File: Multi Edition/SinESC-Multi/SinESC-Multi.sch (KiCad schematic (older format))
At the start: 84 parts, among them J1 Pad_3x2mm, J2 Pad_3x2mm, J3 Pad_3x2mm, J4 Pad_3x2mm, J5 Pad_3x2mm, J6 Pad_1.5mm_Square, Q1 BSC010N04LSI, Q2 BSC010N04LSI, Q3 BSC010N04LSI, Q4 BSC010N04LSI, Q5 BSC010N04LSI, Q6 BSC010N04LSI, U1 STM32F303CBT7, U2 MAX4239AUT, U3 MAX4239AUT, U4 TMC6100-LA, U5 MAX4239AUT, U6 TPS560430XDBVR, Y1 8MHz

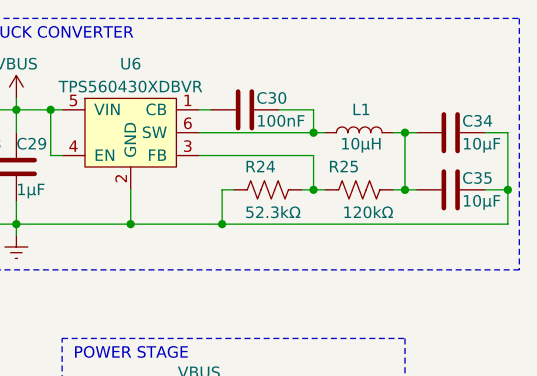
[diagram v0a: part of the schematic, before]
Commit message: Fix issue in the schematic in which the buck converter's 3.3V output is not connected to the rest of the 3.3V rail
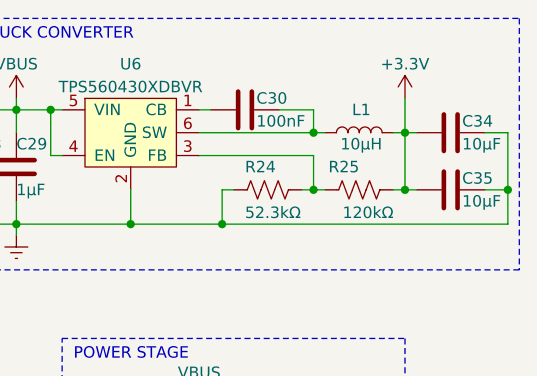
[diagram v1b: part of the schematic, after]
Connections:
- net +3V3: now also C34.2, C35.2, L1.2, R25.2
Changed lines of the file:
@@
 Sheet 1 1
 Title "SinESC Multi Edition"
-Date "2020-09-03"
-Rev "2.3B"
-Comp "Drawn by SAR_mango, © SinESC 2020"
-Comment1 "* All resistors are 1% 0201; current shunts are 1% 1206."
-Comment2 "* Capacitor voltage ratings & packages vary. See BOM."
-Comment3 "* Despite BOM consolidation, E192 values are required."
+Date "2020-12-28"
+Rev "2.3C"
+Comp "Drawn by Erk S., © 2020 SinESC"
+Comment1 "*All resistors are 1% 0201; current shunts are 1% 1206."
+Comment2 "*Capacitor voltage ratings & packages vary. See BOM."
+Comment3 "*Despite BOM consolidation, E192 values are required."
 Comment4 ""
 $EndDescr
@@
 EndData
 $EndBitmap
+$Comp
+L power:+3.3V #PWR?
+U 1 1 5FEB2144
+P 10050 850
+F 0 "#PWR?" H 10050 700 50  0001 C CNN
+F 1 "+3.3V" H 10050 1000 50  0000 C CNN
+F 2 "" H 10050 850 50  0001 C CNN
+F 3 "" H 10050 850 50  0001 C CNN
+	1    10050 850
+	1    0    0    -1
+$EndComp
+Wire Wire Line
+	10050 850  10050 1000
 $EndSCHEMATC

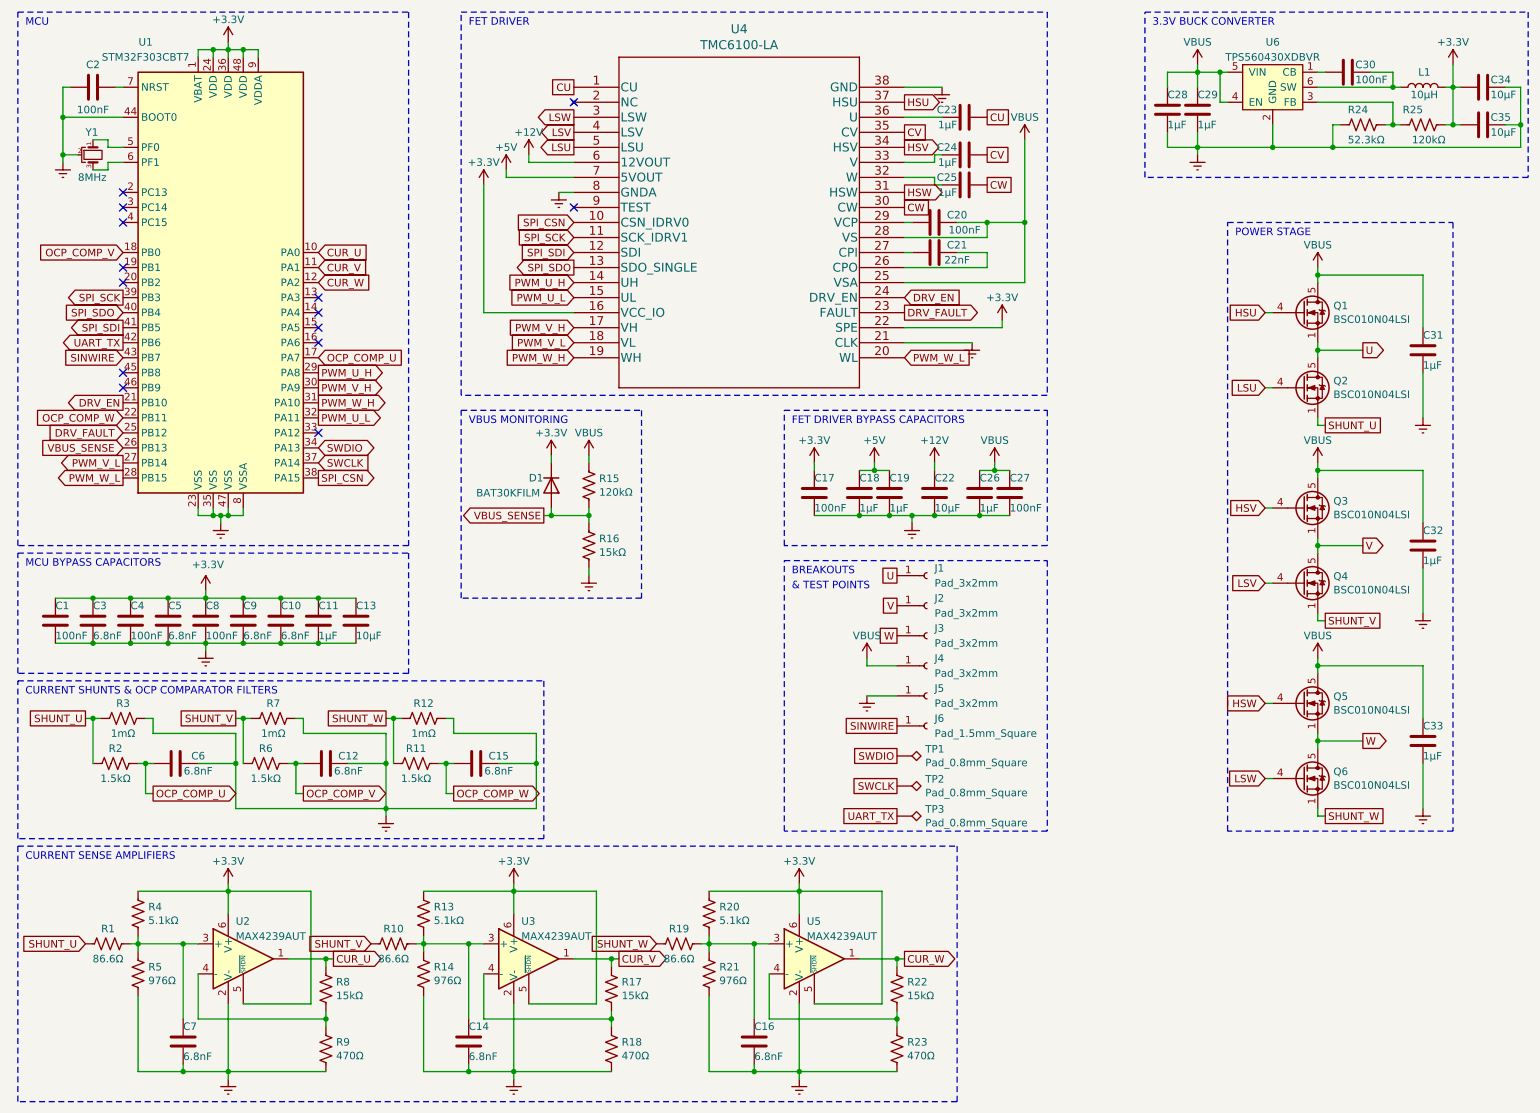
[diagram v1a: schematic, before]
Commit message: Fix another issue in which the bootstrap capacitors were not connected to the source pins of the high-side FETs
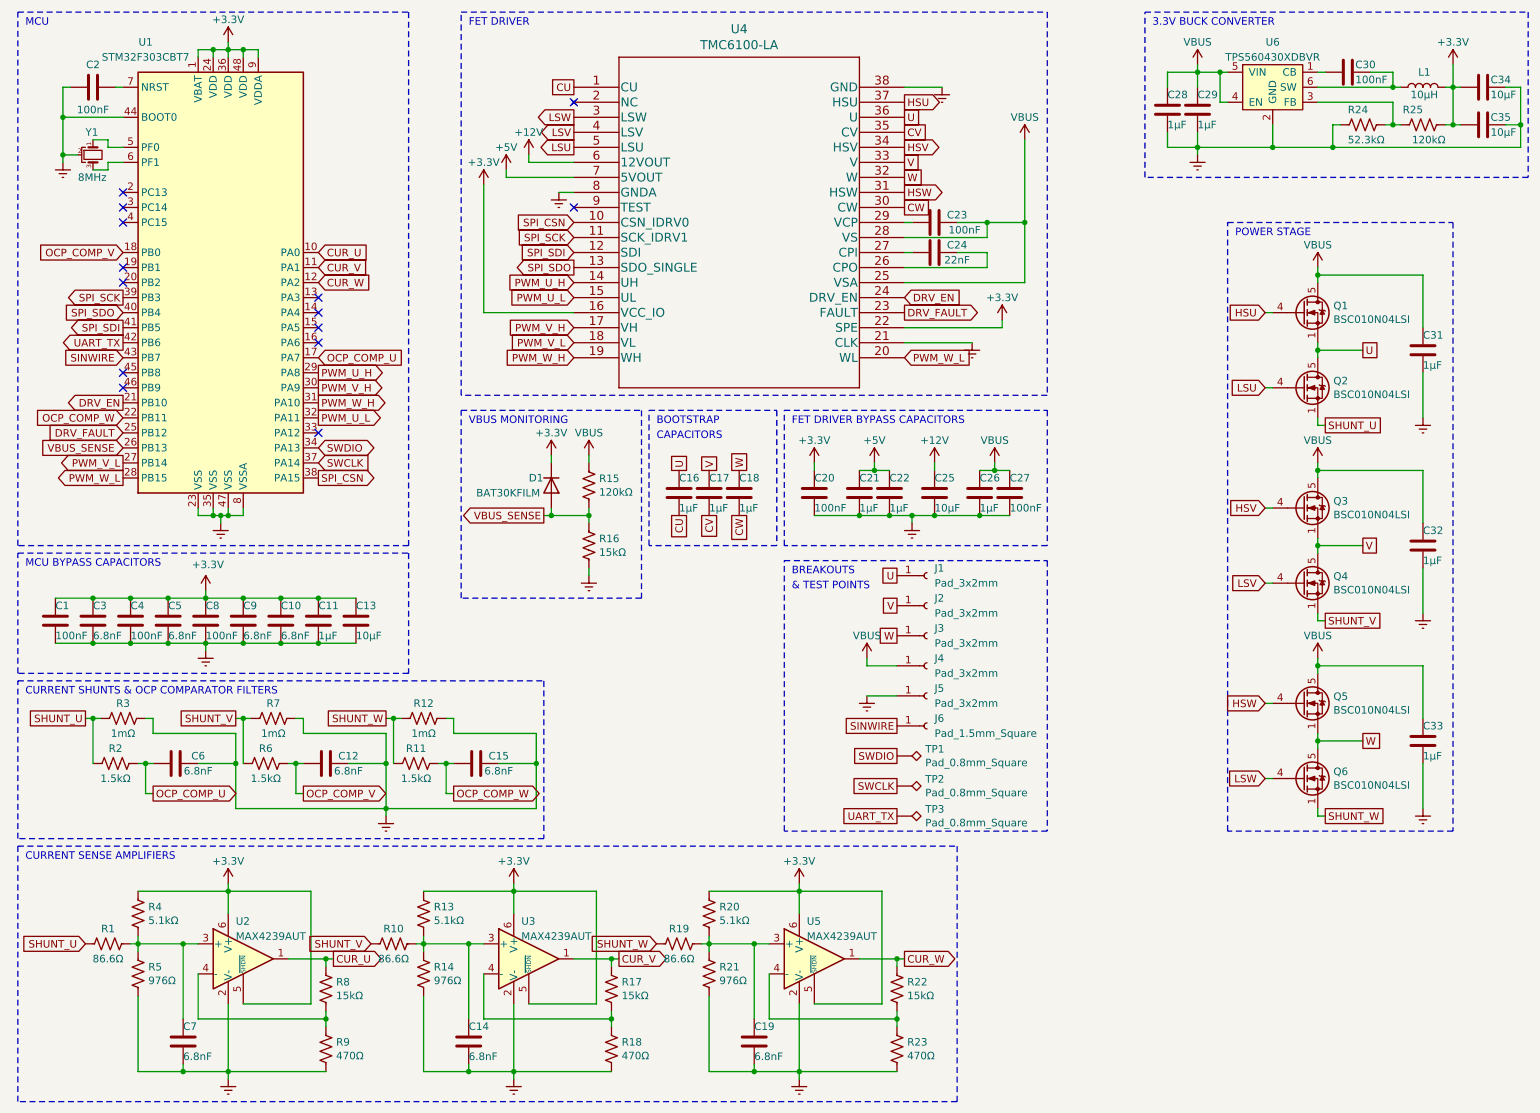
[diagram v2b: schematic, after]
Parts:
- U1: footprint Package_QFP:LQFP-48_7x7mm_P0.5mm -> LQFP-48_7x7mm_P0.5mm_narrow_pads:LQFP-48_7x7mm_P0.5mm_narrow_pads
- renumbered C23 to C16, C24 to C17, C25 to C18, C16 to C19, C17 to C20, C18 to C21, C19 to C22, C20 to C23, C21 to C24, C22 to C25
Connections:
- net U: now also C16.1, U4.36 (U)
- net V: now also C17.1, U4.33 (V)
- net W: now also C18.1, U4.32 (W)
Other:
- note added: "BOOTSTRAP"
- note added: "CAPACITORS"
- moved on the sheet: C16, C17, C18
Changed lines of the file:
@@
 Sheet 1 1
 Title "SinESC Multi Edition"
-Date "2020-12-28"
+Date "2020-12-30"
 Rev "2.3C"
 Comp "Drawn by Erk S., © 2020 SinESC"
@@
 $EndComp
 $Comp
-L Device:C C16
+L Device:C C19
 U 1 1 5F7BA4B1
 P 5400 7350
-F 0 "C16" H 5400 7450 50  0000 L CNN
+F 0 "C19" H 5400 7450 50  0000 L CNN
 F 1 "6.8nF" H 5400 7250 50  0000 L CNN
 F 2 "Capacitor_SMD:C_0201_0603Metric" H 5438 7200 50  0001 C CNN
@@
 $EndComp
 $Comp
-L Device:C C22
+L Device:C C25
 U 1 1 5F4CAC58
 P 6600 3700
-F 0 "C22" H 6600 3800 50  0000 L CNN
+F 0 "C25" H 6600 3800 50  0000 L CNN
 F 1 "10µF" H 6600 3600 50  0000 L CNN
 F 2 "Capacitor_SMD:C_0603_1608Metric" H 6638 3550 50  0001 C CNN
@@
 $EndComp
 $Comp
-L Device:C C19
+L Device:C C22
 U 1 1 5F4CAA4D
 P 6300 3700
-F 0 "C19" H 6300 3800 50  0000 L CNN
+F 0 "C22" H 6300 3800 50  0000 L CNN
 F 1 "1µF" H 6300 3600 50  0000 L CNN
 F 2 "Capacitor_SMD:C_0402_1005Metric" H 6338 3550 50  0001 C CNN
@@
 $EndComp
 $Comp
-L Device:C C18
+L Device:C C21
 U 1 1 5F4CA4EA
 P 6100 3700
-F 0 "C18" H 6100 3800 50  0000 L CNN
+F 0 "C21" H 6100 3800 50  0000 L CNN
 F 1 "1µF" H 6100 3600 50  0000 L CNN
 F 2 "Capacitor_SMD:C_0402_1005Metric" H 6138 3550 50  0001 C CNN
@@
 $EndComp
 $Comp
-L Device:C C17
+L Device:C C20
 U 1 1 5F4C9EF6
 P 5800 3700
-F 0 "C17" H 5800 3800 50  0000 L CNN
+F 0 "C20" H 5800 3800 50  0000 L CNN
 F 1 "100nF" H 5800 3600 50  0000 L CNN
 F 2 "Capacitor_SMD:C_0201_0603Metric" H 5838 3550 50  0001 C CNN
@@
 	6450 2100 6400 2100
 $Comp
-L Device:C C21
+L Device:C C24
 U 1 1 5F488471
 P 6600 2100
-F 0 "C21" V 6550 2250 50  0000 C CNN
+F 0 "C24" V 6550 2250 50  0000 C CNN
 F 1 "22nF" V 6650 2250 50  0000 C CNN
 F 2 "Capacitor_SMD:C_0603_1608Metric" H 6638 1950 50  0001 C CNN
@@
 	6450 1900 6400 1900
 $Comp
-L Device:C C20
+L Device:C C23
 U 1 1 5F47F307
 P 6600 1900
-F 0 "C20" V 6550 2050 50  0000 C CNN
+F 0 "C23" V 6550 2050 50  0000 C CNN
 F 1 "100nF" V 6650 2100 50  0000 C CNN
 F 2 "Capacitor_SMD:C_0201_0603Metric" H 6638 1750 50  0001 C CNN
@@
 Text GLabel 4200 1900 0    50   Input ~ 0
 SPI_CSN
-Wire Wire Line
-	6650 1650 6600 1650
-Wire Wire Line
-	6650 1450 6600 1450
-Wire Wire Line
-	6650 1200 6400 1200
 NoConn ~ 4200 1100
 $Comp
@@
 Text GLabel 4200 1200 0    50   Output ~ 0
 LSW
-Wire Wire Line
-	6600 1600 6400 1600
-Wire Wire Line
-	6600 1650 6600 1600
-Wire Wire Line
-	6600 1500 6600 1450
-Wire Wire Line
-	6400 1500 6600 1500
 Text GLabel 6400 1100 2    50   Output ~ 0
 HSU
@@
 HSV
 $Comp
-L Device:C C24
+L Device:C C17
 U 1 1 5F40C21D
-P 6800 1450
-F 0 "C24" V 6850 1500 50  0000 L CNN
-F 1 "1µF" V 6750 1500 50  0000 L CNN
-F 2 "Capacitor_SMD:C_0402_1005Metric" H 6838 1300 50  0001 C CNN
-F 3 "" H 6800 1450 50  0001 C CNN
-F 4 "50V" H 6800 1450 50  0001 C CNN "Voltage Rating"
-F 5 "UMK105CBJ105MV-F" H 6800 1450 50  0001 C CNN "Manufacturer Part #"
-	1    6800 1450
-	0    -1   -1   0
+P 5100 3700
+F 0 "C17" H 5100 3800 50  0000 L CNN
+F 1 "1µF" H 5100 3600 50  0000 L CNN
+F 2 "Capacitor_SMD:C_0402_1005Metric" H 5138 3550 50  0001 C CNN
+F 3 "" H 5100 3700 50  0001 C CNN
+F 4 "50V" H 5100 3700 50  0001 C CNN "Voltage Rating"
+F 5 "UMK105CBJ105MV-F" H 5100 3700 50  0001 C CNN "Manufacturer Part #"
+	1    5100 3700
+	1    0    0    -1
 $EndComp
-Text GLabel 6950 1450 2    50   UnSpc ~ 0
+Text GLabel 5100 3850 3    50   UnSpc ~ 0
 CV
 $Comp
-L Device:C C25
-U 1 1 5F40BEFD
-P 6800 1650
-F 0 "C25" V 6850 1700 50  0000 L CNN
-F 1 "1µF" V 6750 1700 50  0000 L CNN
-F 2 "Capacitor_SMD:C_0402_1005Metric" H 6838 1500 50  0001 C CNN
-F 3 "" H 6800 1650 50  0001 C CNN
-F 4 "50V" H 6800 1650 50  0001 C CNN "Voltage Rating"
-F 5 "UMK105CBJ105MV-F" H 6800 1650 50  0001 C CNN "Manufacturer Part #"
-	1    6800 1650
-	0    -1   -1   0
-$EndComp
-$Comp
-L Device:C C23
+L Device:C C16
 U 1 1 5F40A651
-P 6800 1200
-F 0 "C23" V 6850 1250 50  0000 L CNN
-F 1 "1µF" V 6750 1250 50  0000 L CNN
-F 2 "Capacitor_SMD:C_0402_1005Metric" H 6838 1050 50  0001 C CNN
-F 3 "" H 6800 1200 50  0001 C CNN
-F 4 "50V" H 6800 1200 50  0001 C CNN "Voltage Rating"
-F 5 "UMK105CBJ105MV-F" H 6800 1200 50  0001 C CNN "Manufacturer Part #"
-	1    6800 1200
-	0    -1   -1   0
+P 4900 3700
+F 0 "C16" H 4900 3800 50  0000 L CNN
+F 1 "1µF" H 4900 3600 50  0000 L CNN
+F 2 "Capacitor_SMD:C_0402_1005Metric" H 4938 3550 50  0001 C CNN
+F 3 "" H 4900 3700 50  0001 C CNN
+F 4 "50V" H 4900 3700 50  0001 C CNN "Voltage Rating"
+F 5 "UMK105CBJ105MV-F" H 4900 3700 50  0001 C CNN "Manufacturer Part #"
+	1    4900 3700
+	1    0    0    -1
 $EndComp
-Text GLabel 6950 1650 2    50   UnSpc ~ 0
+Text GLabel 5300 3850 3    50   UnSpc ~ 0
 CW
-Text GLabel 6950 1200 2    50   UnSpc ~ 0
+Text GLabel 4900 3850 3    50   UnSpc ~ 0
 CU
 Text GLabel 6400 1800 2    50   UnSpc ~ 0
@@
 F 0 "U1" H 1350 3900 50  0000 C CNN
 F 1 "STM32F303CBT7" H 1350 3800 50  0000 C CNN
-F 2 "Package_QFP:LQFP-48_7x7mm_P0.5mm" H 1300 900 50  0001 R CNN
+F 2 "LQFP-48_7x7mm_P0.5mm_narrow_pads:LQFP-48_7x7mm_P0.5mm_narrow_pads" H 1300 900 50  0001 R CNN
 F 3 "" H 1900 2300 50  0001 C CNN
 F 4 "STM32F303CBT7" H 1900 2300 50  0001 C CNN "Manufacturer Part #"
@@
 Wire Wire Line
 	8800 3000 8850 3000
-Text GLabel 9450 2750 2    50   Output ~ 0
+Text GLabel 9450 2750 2    50   UnSpc ~ 0
 U
 Connection ~ 9150 2750
@@
 Wire Wire Line
 	8800 4300 8850 4300
-Text GLabel 9450 4050 2    50   Output ~ 0
+Text GLabel 9450 4050 2    50   UnSpc ~ 0
 V
 Connection ~ 9150 4050
@@
 Wire Wire Line
 	8800 5600 8850 5600
-Text GLabel 9450 5350 2    50   Output ~ 0
+Text GLabel 9450 5350 2    50   UnSpc ~ 0
 W
 Connection ~ 9150 5350
@@
 $EndBitmap
 $Comp
-L power:+3.3V #PWR?
+L power:+3.3V #PWR039
 U 1 1 5FEB2144
 P 10050 850
-F 0 "#PWR?" H 10050 700 50  0001 C CNN
+F 0 "#PWR039" H 10050 700 50  0001 C CNN
 F 1 "+3.3V" H 10050 1000 50  0000 C CNN
 F 2 "" H 10050 850 50  0001 C CNN
@@
 Wire Wire Line
 	10050 850  10050 1000
+$Comp
+L Device:C C18
+U 1 1 5F40BEFD
+P 5300 3700
+F 0 "C18" H 5300 3800 50  0000 L CNN
+F 1 "1µF" H 5300 3600 50  0000 L CNN
+F 2 "Capacitor_SMD:C_0402_1005Metric" H 5338 3550 50  0001 C CNN
+F 3 "" H 5300 3700 50  0001 C CNN
+F 4 "50V" H 5300 3700 50  0001 C CNN "Voltage Rating"
+F 5 "UMK105CBJ105MV-F" H 5300 3700 50  0001 C CNN "Manufacturer Part #"
+	1    5300 3700
+	1    0    0    -1
+$EndComp
+Text GLabel 6400 1200 2    50   UnSpc ~ 0
+U
+Text GLabel 6400 1500 2    50   UnSpc ~ 0
+V
+Text GLabel 6400 1600 2    50   UnSpc ~ 0
+W
+Text GLabel 5300 3550 1    50   UnSpc ~ 0
+W
+Text GLabel 5100 3550 1    50   UnSpc ~ 0
+V
+Text GLabel 4900 3550 1    50   UnSpc ~ 0
+U
+Text Notes 4750 3250 0    50   ~ 0
+BOOTSTRAP
+Text Notes 4750 3350 0    50   ~ 0
+CAPACITORS
+Wire Notes Line
+	4700 3150 5550 3150
+Wire Notes Line
+	5550 3150 5550 4050
+Wire Notes Line
+	5550 4050 4700 4050
+Wire Notes Line
+	4700 4050 4700 3150
 $EndSCHEMATC
